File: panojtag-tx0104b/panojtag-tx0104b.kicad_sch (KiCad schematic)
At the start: 8 parts, among them J1 Conn_01x06, J2 Conn_01x06, U1 TXB0104D

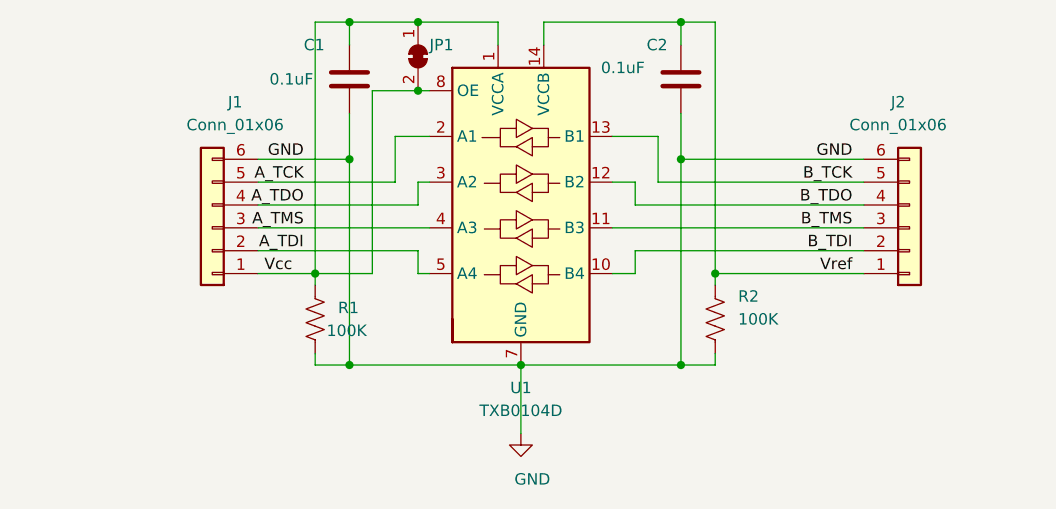
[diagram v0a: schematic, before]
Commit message: Cleaned up and routed TX0104B version, but e're not going to use it. Routed using TopoR with 45deg tracks.
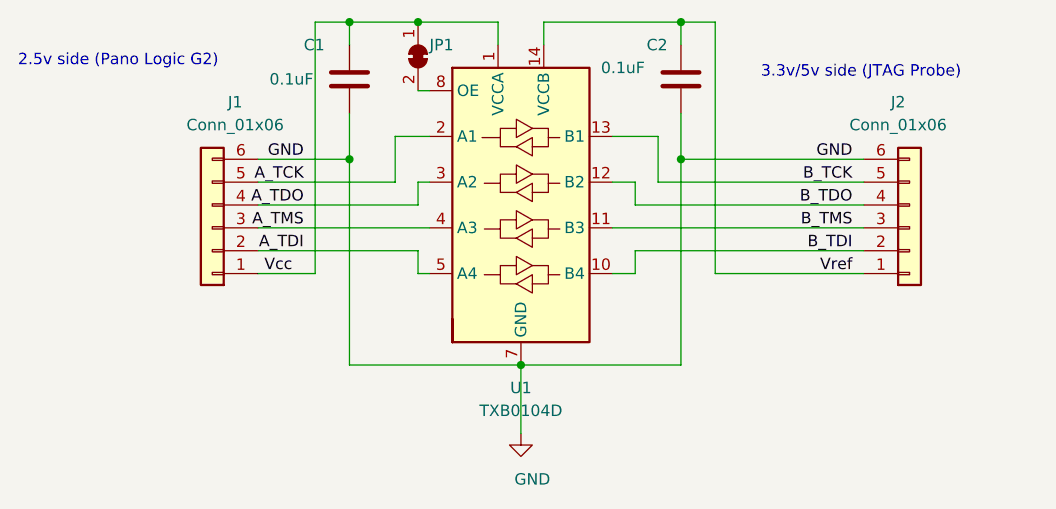
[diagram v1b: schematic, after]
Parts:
- removed R1, R2: 100K, Resistor_SMD:R_0805_2012Metric_Pad1.20x1.40mm_HandSolder, symbol Device:R_US
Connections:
- net Vcc: no longer JP1.2 (B), U1.8 (OE)
- new net: JP1.2 (B), U1.8 (OE)
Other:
- note added: "2.5v side (Pano Logic G2)"
- note added: "3.3v/5v side (JTAG Probe)"
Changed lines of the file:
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@@
 (kicad_sch (version 20210621) (generator eeschema)
   (paper "A4")
-  (junction (at 67.31 105.41) (diameter 0.9144) (color 0 0 0 0))
   (junction (at 71.12 77.47) (diameter 0.9144) (color 0 0 0 0))
   (junction (at 71.12 92.71) (diameter 0.9144) (color 0 0 0 0))
-  (junction (at 71.12 115.57) (diameter 0.9144) (color 0 0 0 0))
   (junction (at 78.74 77.47) (diameter 0.9144) (color 0 0 0 0))
-  (junction (at 78.74 85.09) (diameter 0.9144) (color 0 0 0 0))
   (junction (at 90.17 115.57) (diameter 0.9144) (color 0 0 0 0))
   (junction (at 107.95 77.47) (diameter 0.9144) (color 0 0 0 0))
   (junction (at 107.95 92.71) (diameter 0.9144) (color 0 0 0 0))
-  (junction (at 107.95 115.57) (diameter 0.9144) (color 0 0 0 0))
-  (junction (at 111.76 105.41) (diameter 0.9144) (color 0 0 0 0))
   (wire (pts (xy 60.96 92.71) (xy 71.12 92.71))
     (stroke (width 0) (type solid) (color 0 0 0 0))
@@
     (stroke (width 0) (type solid) (color 0 0 0 0))
   )
-  (wire (pts (xy 67.31 105.41) (xy 67.31 106.68))
-    (stroke (width 0) (type solid) (color 0 0 0 0))
-  )
-  (wire (pts (xy 67.31 114.3) (xy 67.31 115.57))
-    (stroke (width 0) (type solid) (color 0 0 0 0))
-  )
   (wire (pts (xy 71.12 77.47) (xy 71.12 80.01))
     (stroke (width 0) (type solid) (color 0 0 0 0))
@@
     (stroke (width 0) (type solid) (color 0 0 0 0))
   )
-  (wire (pts (xy 71.12 115.57) (xy 67.31 115.57))
-    (stroke (width 0) (type solid) (color 0 0 0 0))
-  )
-  (wire (pts (xy 73.66 85.09) (xy 73.66 105.41))
-    (stroke (width 0) (type solid) (color 0 0 0 0))
-  )
-  (wire (pts (xy 73.66 105.41) (xy 67.31 105.41))
-    (stroke (width 0) (type solid) (color 0 0 0 0))
-  )
   (wire (pts (xy 76.2 90.17) (xy 80.01 90.17))
     (stroke (width 0) (type solid) (color 0 0 0 0))
@@
     (stroke (width 0) (type solid) (color 0 0 0 0))
   )
-  (wire (pts (xy 78.74 85.09) (xy 73.66 85.09))
-    (stroke (width 0) (type solid) (color 0 0 0 0))
-  )
   (wire (pts (xy 78.74 85.09) (xy 80.01 85.09))
     (stroke (width 0) (type solid) (color 0 0 0 0))
@@
     (stroke (width 0) (type solid) (color 0 0 0 0))
   )
-  (wire (pts (xy 107.95 115.57) (xy 111.76 115.57))
-    (stroke (width 0) (type solid) (color 0 0 0 0))
-  )
   (wire (pts (xy 111.76 105.41) (xy 111.76 77.47))
     (stroke (width 0) (type solid) (color 0 0 0 0))
   )
-  (wire (pts (xy 111.76 105.41) (xy 111.76 106.68))
-    (stroke (width 0) (type solid) (color 0 0 0 0))
-  )
   (wire (pts (xy 111.76 105.41) (xy 128.27 105.41))
     (stroke (width 0) (type solid) (color 0 0 0 0))
   )
-  (wire (pts (xy 111.76 115.57) (xy 111.76 114.3))
-    (stroke (width 0) (type solid) (color 0 0 0 0))
-  )
   (wire (pts (xy 128.27 95.25) (xy 105.41 95.25))
     (stroke (width 0) (type solid) (color 0 0 0 0))
@@
   (wire (pts (xy 128.27 102.87) (xy 102.87 102.87))
     (stroke (width 0) (type solid) (color 0 0 0 0))
+  )
+  (text "2.5v side (Pano Logic G2)" (at 34.29 82.55 0)
+    (effects (font (size 1.27 1.27)) (justify left bottom))
+  )
+  (text "3.3v/5v side (JTAG Probe)" (at 116.84 83.82 0)
+    (effects (font (size 1.27 1.27)) (justify left bottom))
   )
   (label "Vcc" (at 64.77 105.41 180)
@@
     (pin "1")
   )
-  (symbol (lib_id "Device:R_US") (at 67.31 110.49 0) (unit 1)
-    (in_bom yes) (on_board yes)
-    (property "Reference" "R1" (id 0) (at 69.85 109.22 0)
-      (effects (font (size 1.27 1.27)) (justify left))
-    )
-    (property "Value" "100K" (id 1) (at 68.58 111.76 0)
-      (effects (font (size 1.27 1.27)) (justify left))
-    )
-    (property "Footprint" "Resistor_SMD:R_0805_2012Metric_Pad1.20x1.40mm_HandSolder" (id 2) (at 68.326 110.744 90)
-      (effects (font (size 1.27 1.27)) hide)
-    )
-    (property "Datasheet" "~" (id 3) (at 67.31 110.49 0)
-      (effects (font (size 1.27 1.27)) hide)
-    )
-    (pin "1")
-    (pin "2")
-  )
   (symbol (lib_id "Jumper:SolderJumper_2_Bridged") (at 78.74 81.28 270) (unit 1)
     (in_bom yes) (on_board yes)
@@
     )
     (property "Datasheet" "~" (id 3) (at 78.74 81.28 0)
-      (effects (font (size 1.27 1.27)) hide)
-    )
-    (pin "1")
-    (pin "2")
-  )
-  (symbol (lib_id "Device:R_US") (at 111.76 110.49 0) (unit 1)
-    (in_bom yes) (on_board yes)
-    (property "Reference" "R2" (id 0) (at 114.3 107.95 0)
-      (effects (font (size 1.27 1.27)) (justify left))
-    )
-    (property "Value" "100K" (id 1) (at 114.3 110.49 0)
-      (effects (font (size 1.27 1.27)) (justify left))
-    )
-    (property "Footprint" "Resistor_SMD:R_0805_2012Metric_Pad1.20x1.40mm_HandSolder" (id 2) (at 112.776 110.744 90)
-      (effects (font (size 1.27 1.27)) hide)
-    )
-    (property "Datasheet" "~" (id 3) (at 111.76 110.49 0)
       (effects (font (size 1.27 1.27)) hide)
     )
@@
       (reference "JP1") (unit 1) (value "SolderJumper_2_Bridged") (footprint "Jumper:SolderJumper-2_P1.3mm_Bridged_Pad1.0x1.5mm")
     )
-    (path "/8b40913a-f9a3-4d3a-be90-00fd300f9bea"
-      (reference "R1") (unit 1) (value "100K") (footprint "Resistor_SMD:R_0805_2012Metric_Pad1.20x1.40mm_HandSolder")
-    )
-    (path "/d438449a-b2a4-49fd-bee0-4b435670ff86"
-      (reference "R2") (unit 1) (value "100K") (footprint "Resistor_SMD:R_0805_2012Metric_Pad1.20x1.40mm_HandSolder")
-    )
     (path "/aa584c9f-3b74-40be-8e5e-bee73fa8caea"
